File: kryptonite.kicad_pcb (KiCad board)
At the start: 2 copper layers, 4 parts, among them U1 STM32F072CBUx, U2 ATECC608A-MAHDA, U3 MCP1700x-330xxTT, Y1 Crystal_GND24

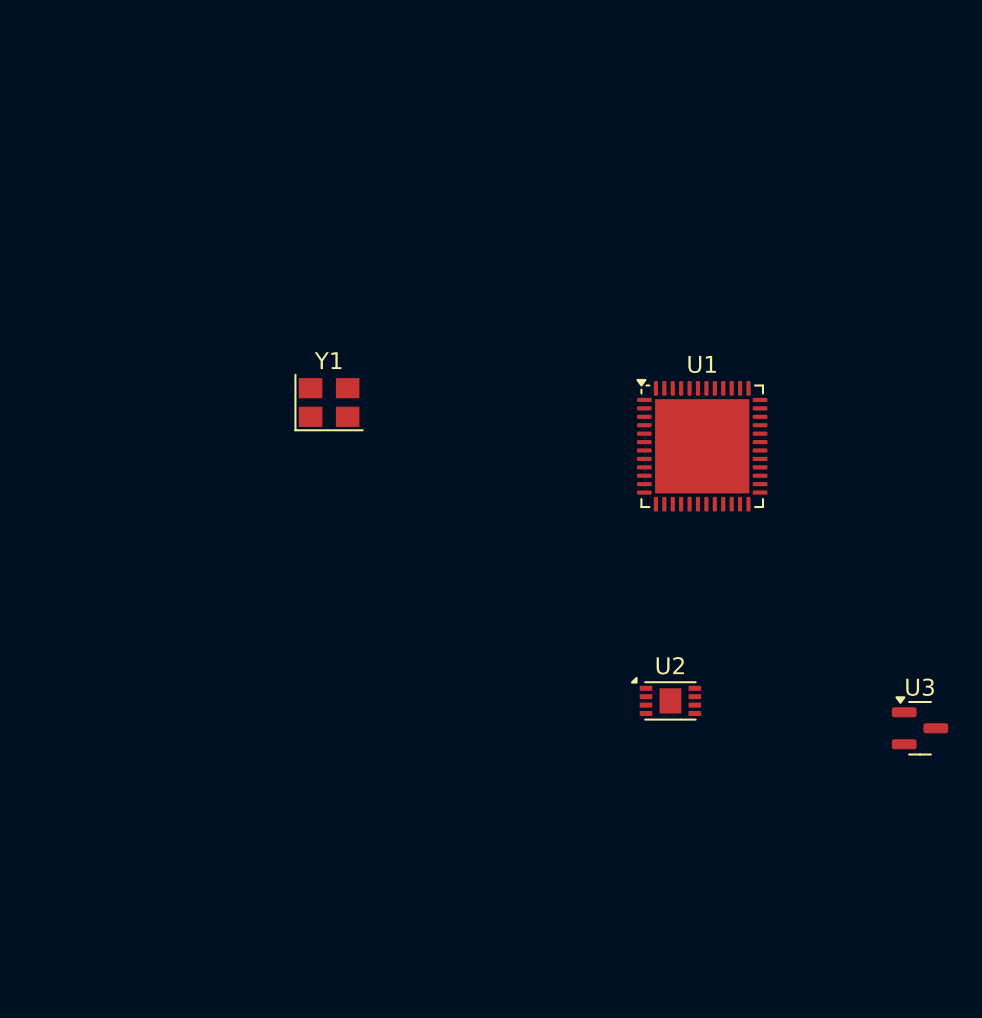
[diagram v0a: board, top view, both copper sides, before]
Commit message: Added ESD protection
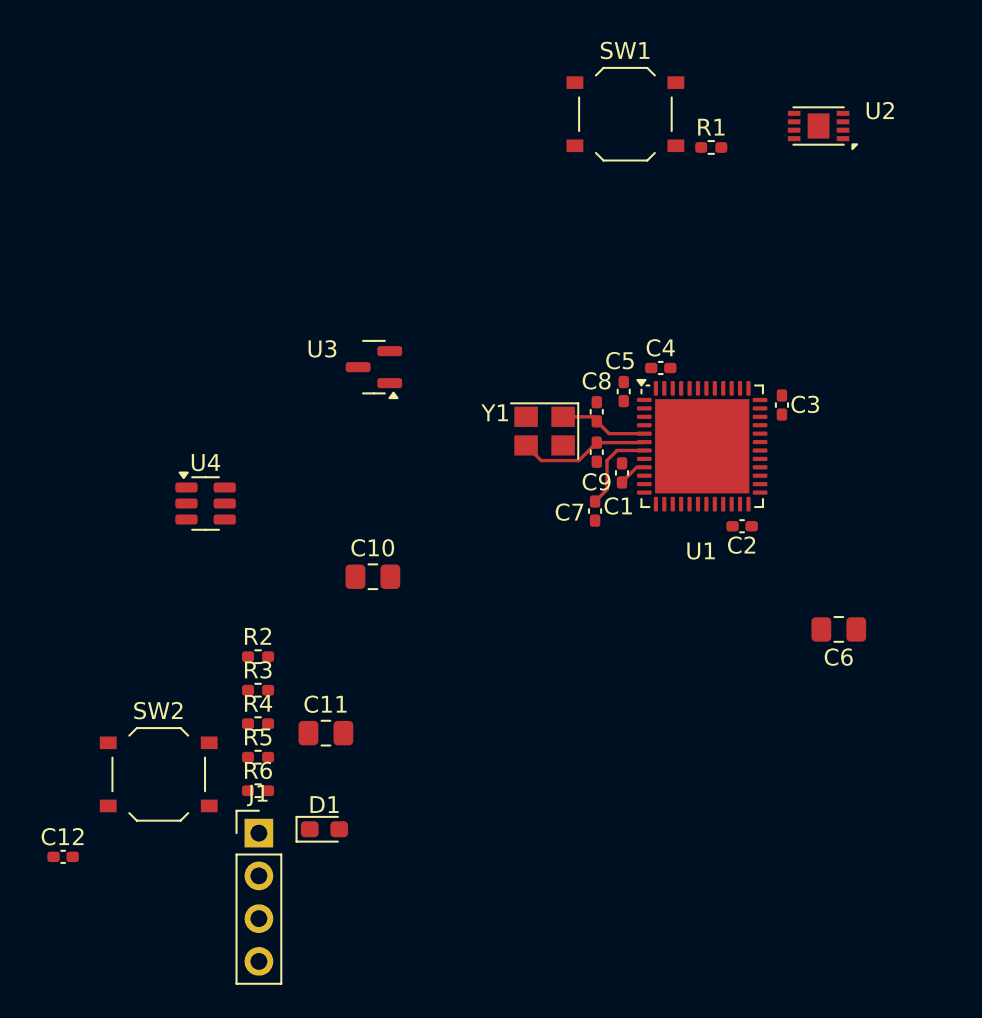
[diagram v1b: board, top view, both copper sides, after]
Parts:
- added C1: 100n, Capacitor_SMD:C_0402_1005Metric_Pad0.74x0.62mm_HandSolder, F.Cu at (94.3, 61.8)
- added C10: 1u, Capacitor_SMD:C_0805_2012Metric_Pad1.18x1.45mm_HandSolder, F.Cu at (79.5, 68.0)
- added C11: 1u, Capacitor_SMD:C_0805_2012Metric_Pad1.18x1.45mm_HandSolder, F.Cu at (76.7, 77.3)
- added C12: 100n, Capacitor_SMD:C_0402_1005Metric_Pad0.74x0.62mm_HandSolder, F.Cu at (61.1, 84.6)
- added C2: 100n, Capacitor_SMD:C_0402_1005Metric_Pad0.74x0.62mm_HandSolder, F.Cu at (101.4, 65.0)
- added C3: 100n, Capacitor_SMD:C_0402_1005Metric_Pad0.74x0.62mm_HandSolder, F.Cu at (103.8, 57.8)
- added C4: 100n, Capacitor_SMD:C_0402_1005Metric_Pad0.74x0.62mm_HandSolder, F.Cu at (96.6, 55.6)
- added C5: 100n, Capacitor_SMD:C_0402_1005Metric_Pad0.74x0.62mm_HandSolder, F.Cu at (94.4, 57.0)
- added C6: 10u, Capacitor_SMD:C_0805_2012Metric_Pad1.18x1.45mm_HandSolder, F.Cu at (107.2, 71.1)
- added C7: 100n, Capacitor_SMD:C_0402_1005Metric_Pad0.74x0.62mm_HandSolder, F.Cu at (92.7, 64.1)
- added C8: 33p, Capacitor_SMD:C_0402_1005Metric_Pad0.74x0.62mm_HandSolder, F.Cu at (92.8, 58.2)
- added C9: 33p, Capacitor_SMD:C_0402_1005Metric_Pad0.74x0.62mm_HandSolder, F.Cu at (92.8, 60.6)
- added D1: GR, LED_SMD:LED_0603_1608Metric_Pad1.05x0.95mm_HandSolder, F.Cu at (76.6, 83.0)
- added J1: Conn_01x04_Pin, Connector_PinHeader_2.54mm:PinHeader_1x04_P2.54mm_Vertical, F.Cu at (72.7, 83.2)
- added R1: 10k, Resistor_SMD:R_0402_1005Metric_Pad0.72x0.64mm_HandSolder, F.Cu at (99.6, 42.5)
- added R2: 4k7, Resistor_SMD:R_0402_1005Metric_Pad0.72x0.64mm_HandSolder, F.Cu at (72.7, 72.8)
- added R3: 4k7, Resistor_SMD:R_0402_1005Metric_Pad0.72x0.64mm_HandSolder, F.Cu at (72.7, 74.7)
- added R4: 4k7, Resistor_SMD:R_0402_1005Metric_Pad0.72x0.64mm_HandSolder, F.Cu at (72.7, 76.7)
- added R5: 2k2, Resistor_SMD:R_0402_1005Metric_Pad0.72x0.64mm_HandSolder, F.Cu at (72.7, 78.7)
- added R6: 10k, Resistor_SMD:R_0402_1005Metric_Pad0.72x0.64mm_HandSolder, F.Cu at (72.7, 80.7)
- added SW1: SW_Push, Button_Switch_SMD:SW_Push_1P1T_XKB_TS-1187A, F.Cu at (94.5, 40.5)
- added SW2: SW_Push, Button_Switch_SMD:SW_Push_1P1T_XKB_TS-1187A, F.Cu at (66.8, 79.7)
- added U4: USBLC6-2SC6, Package_TO_SOT_SMD:SOT-23-6, F.Cu at (69.6, 63.6)
- U2: value ATECC608A-MAHDA -> ATECC608B-MAHDA
- Y1: value Crystal_GND24 -> 8MHz
- moved U3 38.9 mm to (79.6, 55.5), turned to 180 degrees
- moved U2 35.3 mm to (106.0, 41.2), turned to 180 degrees
- moved Y1 12.9 mm to (89.7, 59.4), turned to 180 degrees
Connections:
- U1 pad 11: unconnected-(U1-PA1-Pad11) -> /Btn
- U1 pad 12: unconnected-(U1-PA2-Pad12) -> /LED_A
- U1 pad 32: /USB_D- -> USB_D-
- U1 pad 33: /USB_D+ -> USB_D+
- U1 pad 42: /SCL -> unconnected-(U1-PB6-Pad42)
- U1 pad 45: unconnected-(U1-PB8-Pad45) -> /SCL
- U2 pad 4: unconnected-(U2-GND-Pad4) -> GND
- U2 pad 5: unconnected-(U2-SDA-Pad5) -> /SDA
- U2 pad 6: unconnected-(U2-SCL-Pad6) -> /SCL
- U2 pad 8: unconnected-(U2-VCC-Pad8) -> +3V3
- U2 pad 9: unconnected-(U2-EP-Pad9) -> GND
- U3 pad 1: unconnected-(U3-GND-Pad1) -> GND
- U3 pad 2: unconnected-(U3-VO-Pad2) -> +3V3
- U3 pad 3: unconnected-(U3-VI-Pad3) -> VBUS
- Y1 pad 1: unconnected-(Y1-Pad1) -> /HSE_IN
- Y1 pad 2: unconnected-(Y1-Pad2) -> GND
- Y1 pad 3: unconnected-(Y1-Pad3) -> /HSE_OUT
- Y1 pad 4: unconnected-(Y1-Pad4) -> GND
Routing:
- net /HSE_OUT: track 0.00 -> 7.85 mm
- net /HSE_IN: track 0.00 -> 5.24 mm
- net /NRST: track 0.00 -> 5.20 mm
- net +3V3: track 0.00 -> 1.71 mm

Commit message: did some stuff
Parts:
- removed SW2: SW_Push, Button_Switch_SMD:SW_Push_1P1T_XKB_TS-1187A
- added P1: USB_C_Plug_USB2.0, type-c:TYPE-C-31-G-01, F.Cu at (112.8, 60.6)
- C1, C12: value 100n -> 10u; footprint Capacitor_SMD:C_0402_1005Metric_Pad0.74x0.62mm_HandSolder -> Capacitor_SMD:C_0603_1608Metric
- C10: value 1u -> 100n; footprint Capacitor_SMD:C_0805_2012Metric_Pad1.18x1.45mm_HandSolder -> Capacitor_SMD:C_0402_1005Metric
- C11: value 1u -> 10u; footprint Capacitor_SMD:C_0805_2012Metric_Pad1.18x1.45mm_HandSolder -> Capacitor_SMD:C_0603_1608Metric
- C2, C3, C4, C5, C7, C8, C9: footprint Capacitor_SMD:C_0402_1005Metric_Pad0.74x0.62mm_HandSolder -> Capacitor_SMD:C_0402_1005Metric
- C6: value 10u -> 100n; footprint Capacitor_SMD:C_0805_2012Metric_Pad1.18x1.45mm_HandSolder -> Capacitor_SMD:C_0402_1005Metric
- D1, SW1: moved to B.Cu
- R1, R2, R3, R4: footprint Resistor_SMD:R_0402_1005Metric_Pad0.72x0.64mm_HandSolder -> Resistor_SMD:R_0402_1005Metric
- R5: value 2k2 -> 10k; footprint Resistor_SMD:R_0402_1005Metric_Pad0.72x0.64mm_HandSolder -> Resistor_SMD:R_0402_1005Metric
- R6: value 10k -> 68; footprint Resistor_SMD:R_0402_1005Metric_Pad0.72x0.64mm_HandSolder -> Resistor_SMD:R_0402_1005Metric
- moved C12 50.6 mm to (109.3, 69.2), turned to -90 degrees
- moved R5 46.8 mm to (110.9, 51.7), turned to 90 degrees
- moved J1 43.3 mm to (106.0, 55.6), turned to -90 degrees
- moved R4 40.6 mm to (109.4, 59.4)
- moved C11 38.0 mm to (113.9, 69.4), turned to -90 degrees
- moved U3 36.5 mm to (111.7, 72.8), turned to 0 degrees
- moved U4 36.5 mm to (105.9, 60.6), turned to 180 degrees
- moved R2 35.3 mm to (94.8, 45.2)
- moved R3 35.3 mm to (94.8, 47.2)
- moved U2 29.5 mm to (90.1, 66.1), turned to 0 degrees
- moved D1 26.2 mm to (91.4, 61.3), turned to -90 degrees
- moved R6 23.8 mm to (94.0, 70.2)
- moved C10 22.5 mm to (89.6, 47.9)
- moved SW1 21.1 mm to (96.3, 61.5), turned to 180 degrees
- moved C6 19.5 mm to (93.9, 56.9), turned to 0 degrees
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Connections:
- C10 pad 1: VBUS -> +3V3
- C11 pad 1: +3V3 -> VBUS
- R1 pad 1: /BOOT0 -> GND
- R1 pad 2: GND -> /BOOT0
- R5 pad 1: GND -> /BTN
- R5 pad 2: /LED_K -> +3V3
- R6 pad 1: /Btn -> GND
- R6 pad 2: +3V3 -> /LED_K
- SW1 pad 1: +3V3 -> /BTN
- SW1 pad 2: /BOOT0 -> GND
- U1 pad 11: /Btn -> unconnected-(U1-PA1-Pad11)
- U1 pad 12: /LED_A -> unconnected-(U1-PA2-Pad12)
- U1 pad 15: unconnected-(U1-PA5-Pad15) -> /LED_A
- U1 pad 16: unconnected-(U1-PA6-Pad16) -> /BTN
- U1 pad 21: unconnected-(U1-PB10-Pad21) -> /SCL
- U1 pad 22: unconnected-(U1-PB11-Pad22) -> /SDA
- U1 pad 43: /SDA -> unconnected-(U1-PB7-Pad43)
- U1 pad 45: /SCL -> unconnected-(U1-PB8-Pad45)
- U4 pad 1: USB_CONN_+ -> USB_CONN_D-
- U4 pad 3: USB_D+ -> USB_CONN_D+
- U4 pad 4: USB_D- -> USB_D+
- U4 pad 6: USB_CONN_D- -> USB_D-
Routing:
- net /HSE_OUT: track 7.85 -> 0.00 mm
- net /HSE_IN: track 5.24 -> 0.00 mm
- net /NRST: track 5.20 -> 0.00 mm
- net +3V3: track 1.71 -> 0.00 mm
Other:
- board outline added: 4 x 8 mm
- copper layers 2 -> 4

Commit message: Add files via upload
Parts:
- D1: moved to F.Cu
- moved R5 34.4 mm to (80.1, 67.0), turned to 0 degrees
- moved C10 18.5 mm to (91.7, 66.3), turned to 180 degrees
- moved R6 16.2 mm to (78.3, 66.3), turned to 90 degrees
- moved D1 12.3 mm to (79.5, 64.4)
- moved U3 10.4 mm to (104.8, 65.0)
- moved C12 8.38 mm to (101.3, 66.4), turned to 180 degrees
- moved C11 6.72 mm to (107.5, 67.1)
- moved R1 6.34 mm to (95.6, 56.4), turned to -90 degrees
- moved U2 5.32 mm to (95.3, 67.3)
- moved C1 2.24 mm to (101.3, 64.2), turned to -90 degrees
- moved P1 1.94 mm to (111.1, 61.5)
- moved R4 1.69 mm to (107.7, 59.2)
- moved U4 1.52 mm to (104.7, 61.5)
- moved C4 0.06 mm to (98.9, 66.2)
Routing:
- net GND: track 0.00 -> 4.75 mm
- net USB_D+: track 0.00 -> 4.51 mm
- net USB_D-: track 0.00 -> 4.51 mm
- net /SDA: track 0.00 -> 4.02 mm
- net USB_CONN_D-: track 0.00 -> 3.51 mm
- net USB_CONN_D+: track 0.00 -> 3.51 mm
- net /NRST: track 0.00 -> 3.39 mm
- net /SCL: track 0.00 -> 3.33 mm
- net /BOOT0: track 0.00 -> 1.18 mm
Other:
- outline, holes or cut-outs redrawn

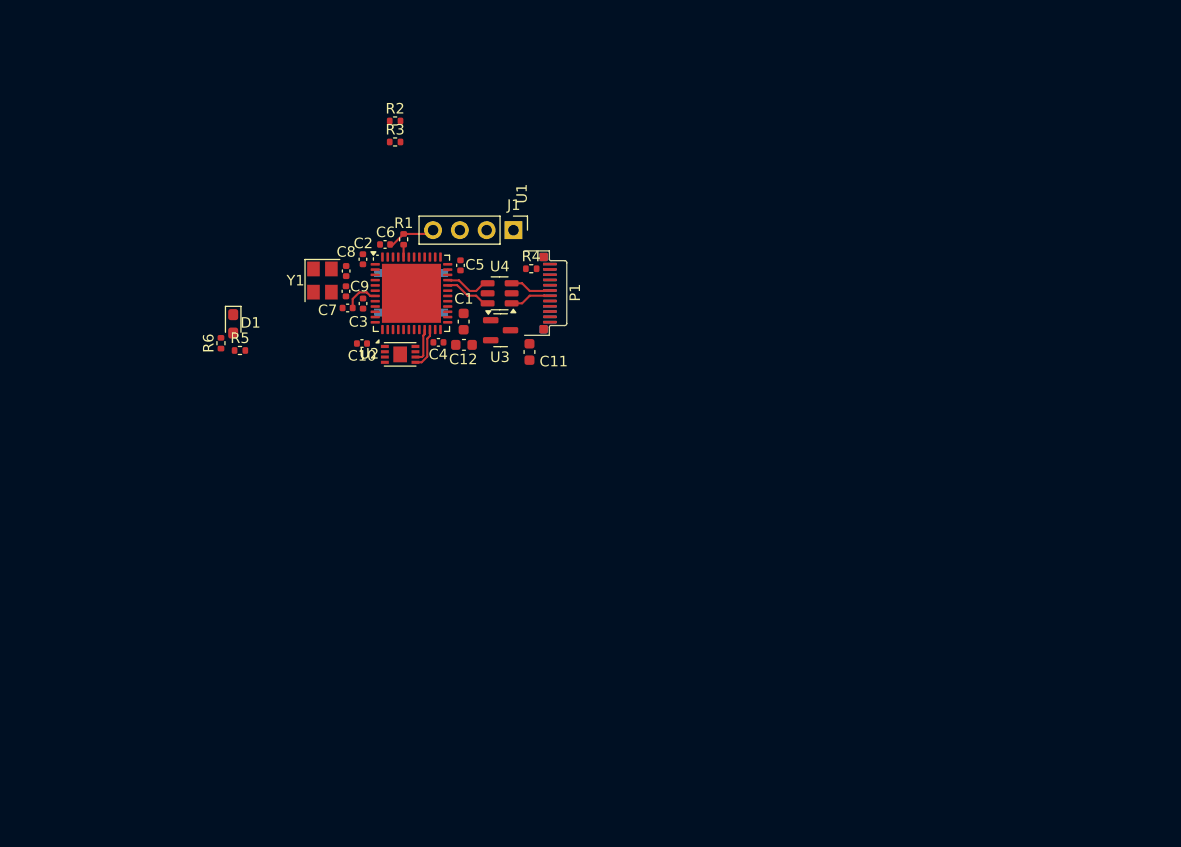
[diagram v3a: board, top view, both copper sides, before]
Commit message: Finalized PCB layout and added gerbers
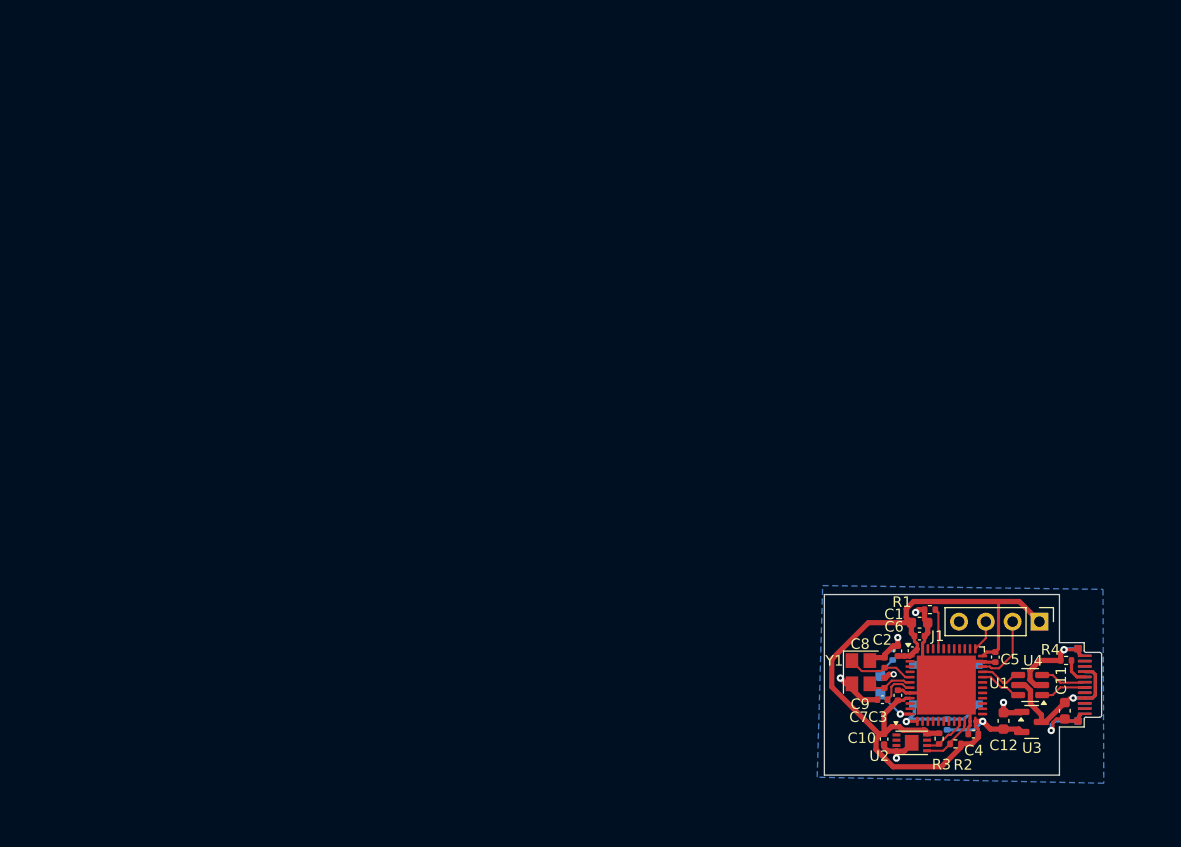
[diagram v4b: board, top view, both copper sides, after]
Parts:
- C8, C9: footprint Capacitor_SMD:C_0402_1005Metric -> Capacitor_SMD:C_0402_1005Metricf
- D1, R5: moved to B.Cu
- R6: footprint Resistor_SMD:R_0402_1005Metric -> Resistor_SMD:R_0402_1005Metricf; moved to B.Cu
- moved R2 79.4 mm to (147.9, 104.3), turned to 180 degrees
- moved R3 76.6 mm to (146.4, 103.8), turned to -90 degrees
- moved R5 75.8 mm to (147.2, 102.4), turned to -90 degrees
- moved D1 70.3 mm to (140.8, 98.7)
- moved R6 70.2 mm to (142.0, 95.8), turned to -90 degrees
- moved C8 63.1 mm to (141.2, 96.6)
- moved Y1 63.1 mm to (139.0, 97.5)
- moved C9 63.1 mm to (141.2, 98.5)
- moved C7 62.9 mm to (141.0, 100.1)
- moved P1 62.9 mm to (161.8, 98.7)
- moved R4 62.9 mm to (158.4, 96.4)
- moved C2 62.9 mm to (142.5, 95.5)
- moved C3 62.9 mm to (142.5, 99.7)
- moved C4 62.9 mm to (149.6, 103.3)
- moved C5 62.9 mm to (151.7, 96.0)
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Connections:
- U1 pad 12: unconnected-(U1-PA2-Pad12) -> /LED_A
- U1 pad 13: unconnected-(U1-PA3-Pad13) -> /BTN
- U1 pad 15: /LED_A -> unconnected-(U1-PA5-Pad15)
- U1 pad 16: /BTN -> unconnected-(U1-PA6-Pad16)
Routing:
- net +3V3: track 0.00 -> 79.8 mm, vias 0 -> 1
- net GND: track 4.75 -> 50.1 mm, vias 0 -> 8
- net VBUS: track 0.00 -> 18.9 mm, vias 0 -> 1
- net /BTN: track 0.00 -> 16.4 mm, vias 0 -> 1
- net /SWDIO: track 0.00 -> 6.58 mm
- net /HSE_IN: track 0.00 -> 6.41 mm
- net /HSE_OUT: track 0.00 -> 3.77 mm
- net /LED_A: track 0.00 -> 3.60 mm, vias 0 -> 1
- net /SWCLK: track 0.00 -> 2.99 mm
- net /BOOT0: track 1.18 -> 3.83 mm
- net Net-(P1-CC): track 0.00 -> 2.51 mm
- net /LED_K: track 0.00 -> 1.65 mm
- net /SDA: track 4.02 -> 5.03 mm
- net USB_D-: track 4.51 -> 3.73 mm
- net USB_D+: track 4.51 -> 3.73 mm
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- added copper zone on B.Cu, net GND
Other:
- board size 4 x 8 mm -> 22.3 x 17.1 mm
- copper layers 4 -> 2
- board text added: "2024-15 V0.1"
- board text added: "3V3"
- board text added: "GND"
- board text added: "SWCLK"
- board text added: "SWDIO"
- board text added: "samienr.com"

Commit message: Add files via upload
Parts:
- C8, C9: footprint Capacitor_SMD:C_0402_1005Metricf -> Capacitor_SMD:C_0402_1005Metric
- R6: footprint Resistor_SMD:R_0402_1005Metricf -> Resistor_SMD:R_0402_1005Metric
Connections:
- P1 pad A6: USB_CONN_D+ -> (no net)
- P1 pad A7: USB_CONN_D- -> (no net)
- U4 pad 1: USB_CONN_D- -> /USB_CONN_D-
- U4 pad 3: USB_CONN_D+ -> /USB_CONN_D+
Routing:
- net USB_CONN_D+: track 4.09 -> 0.00 mm
- net /USB_CONN_D+: track 0.00 -> 4.09 mm
- net USB_CONN_D-: track 4.09 -> 0.00 mm
- net /USB_CONN_D-: track 0.00 -> 4.09 mm
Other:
- board text added: "2024-15 Kryptonite V0.1"
- board text removed: "2024-15 V0.1"
- board text removed: "samienr.com"
